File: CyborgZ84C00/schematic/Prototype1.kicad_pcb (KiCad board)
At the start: 2 copper layers, 4 parts, among them U1 Z84C00, U2 ATmega4809-P, U3 HM628128

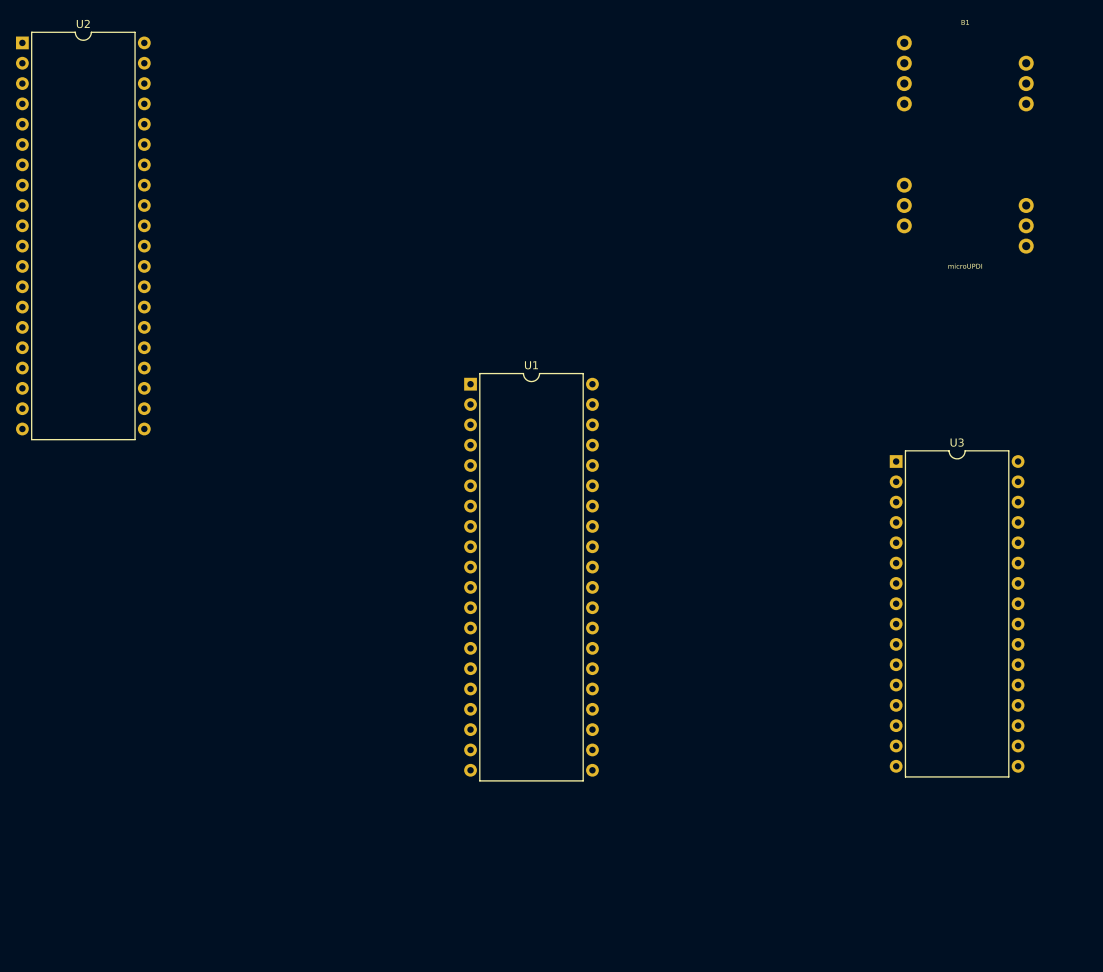
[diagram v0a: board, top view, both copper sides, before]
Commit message: [CyborgZ84C00] Update schematics symbols
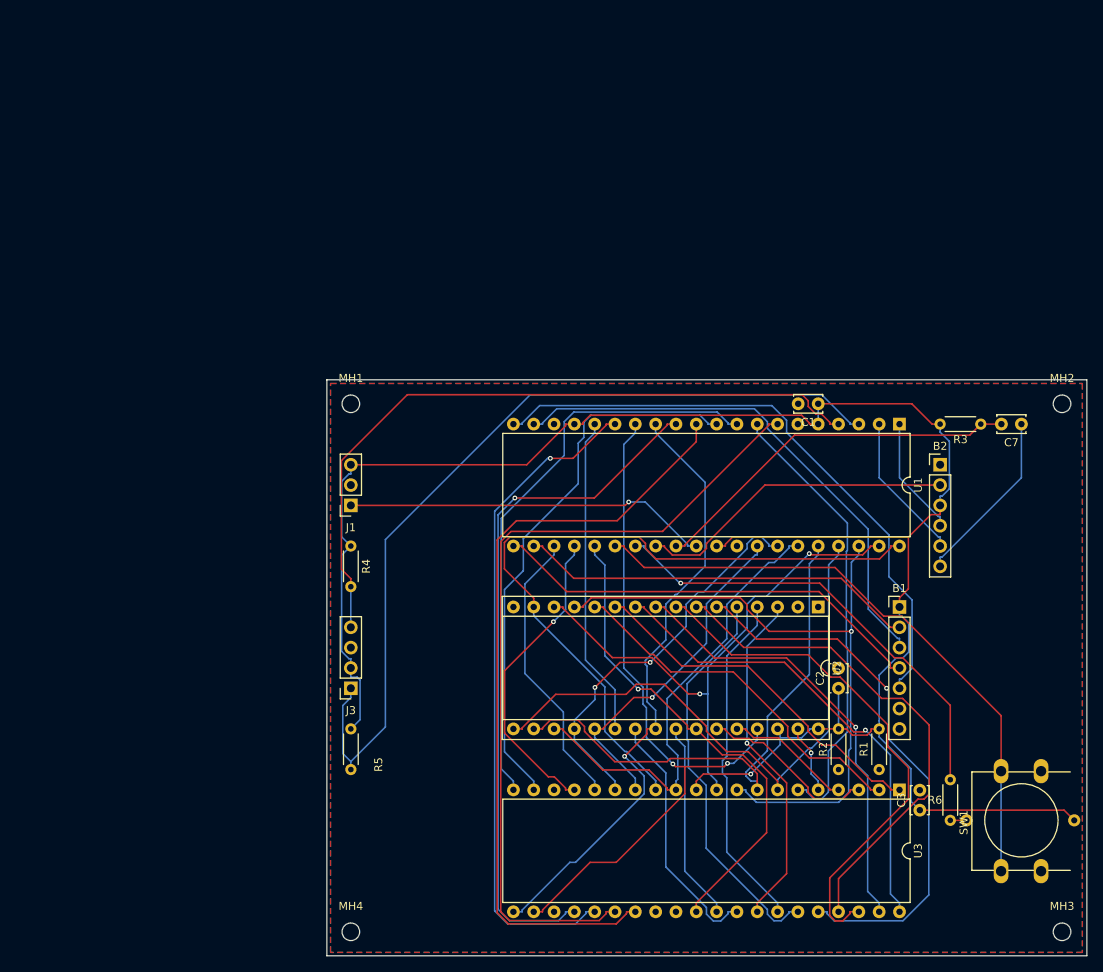
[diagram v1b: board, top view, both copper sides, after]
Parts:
- added B2: USB_Serial, 0-LocalLibrary:GY232V2, F.Cu at (174.7, 77.6)
- added C1: 0.1u, Capacitor_THT:C_Disc_D3.4mm_W2.1mm_P2.50mm, F.Cu at (159.4, 70.0)
- added C2: 0.1u, Capacitor_THT:C_Disc_D3.4mm_W2.1mm_P2.50mm, F.Cu at (162.0, 105.6)
- added C3: 0.1u, Capacitor_THT:C_Disc_D3.4mm_W2.1mm_P2.50mm, F.Cu at (172.1, 120.8)
- added C7: 0.1u, Capacitor_THT:C_Disc_D3.4mm_W2.1mm_P2.50mm, F.Cu at (184.8, 72.5)
- added J1: Conn_AVR_UPDI, Connector_PinSocket_2.54mm:PinSocket_1x03_P2.54mm_Vertical, F.Cu at (101.0, 82.7)
- added J3: Conn_I2C_Master, Connector_PinSocket_2.54mm:PinSocket_1x04_P2.54mm_Vertical, F.Cu at (101.0, 105.6)
- added MH1: MountingHole_2.2mm_M2, MountingHole:MountingHole_2.2mm_M2, F.Cu at (101.0, 70.0)
- added MH2: MountingHole_2.2mm_M2, MountingHole:MountingHole_2.2mm_M2, F.Cu at (189.9, 70.0)
- added MH3: MountingHole_2.2mm_M2, MountingHole:MountingHole_2.2mm_M2, F.Cu at (189.9, 136.0)
- added MH4: MountingHole_2.2mm_M2, MountingHole:MountingHole_2.2mm_M2, F.Cu at (101.0, 136.0)
- added R1: 10k, Resistor_THT:R_Axial_DIN0204_L3.6mm_D1.6mm_P5.08mm_Horizontal, F.Cu at (167.0, 115.7)
- added R2: 10k, Resistor_THT:R_Axial_DIN0204_L3.6mm_D1.6mm_P5.08mm_Horizontal, F.Cu at (162.0, 115.7)
- added R3: 10k, Resistor_THT:R_Axial_DIN0204_L3.6mm_D1.6mm_P5.08mm_Horizontal, F.Cu at (179.7, 72.5)
- added R4: 4k7, Resistor_THT:R_Axial_DIN0204_L3.6mm_D1.6mm_P5.08mm_Horizontal, F.Cu at (101.0, 87.8)
- added R5: 4k7, Resistor_THT:R_Axial_DIN0204_L3.6mm_D1.6mm_P5.08mm_Horizontal, F.Cu at (101.0, 110.6)
- added R6: 560, Resistor_THT:R_Axial_DIN0204_L3.6mm_D1.6mm_P5.08mm_Horizontal, F.Cu at (175.9, 122.1)
- added SW1: TSD1265, 0-LocalLibrary:SW_PUSH-LED-12mm, F.Cu at (182.3, 128.4)
- B1: value microUPDI -> Micro_SD; footprint 0-LocalLibrary:microUPDI -> 0-LocalLibrary:uSD_CARD
- U1: value Z84C00 -> ATmega4809-P
- U2: value ATmega4809-P -> HM628128DLP-5; footprint Package_DIP:DIP-40_W15.24mm -> Package_DIP:DIP-32_W15.24mm_Socket
- U3: value HM628128 -> Z84C00; footprint Package_DIP:DIP-32_W15.24mm -> Package_DIP:DIP-40_W15.24mm
- moved U2 121.9 mm to (159.4, 95.4), turned to 270 degrees
- moved B1 58.4 mm to (169.6, 95.4)
- moved U1 53.9 mm to (169.6, 72.5), turned to 270 degrees
- moved U3 41.0 mm to (169.6, 118.3), turned to 270 degrees
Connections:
- B1 pad 1: (no net) -> VCC
- B1 pad 2: (no net) -> /~SD_CS~
- B1 pad 3: (no net) -> /SD_DI
- B1 pad 4: (no net) -> /SD_SCK
- U1 pad 1: (no net) -> /DBG_RX
- U1 pad 10: (no net) -> /~MREQ~
- U1 pad 11: (no net) -> /~M1~
- U1 pad 12: (no net) -> /~WAIT~
- U1 pad 13: (no net) -> /~RD~
- U1 pad 14: (no net) -> /~WR~
- U1 pad 15: (no net) -> /~BUSREQ~
- U1 pad 16: (no net) -> /~RAM_E~
- U1 pad 17: (no net) -> VCC
- U1 pad 18: (no net) -> GND
- U1 pad 19: (no net) -> /SD_DI
- U1 pad 2: (no net) -> /DBG_TX
- U1 pad 20: (no net) -> /SD_DO
- U1 pad 21: (no net) -> /SD_SCK
- U1 pad 22: (no net) -> /~SD_CS~
- U1 pad 23: (no net) -> /~INT~
- U1 pad 24: (no net) -> /~NMI~
- U1 pad 25: (no net) -> /A0
- U1 pad 26: (no net) -> /~USR_SW~
- U1 pad 27: (no net) -> /~USR_LED~
- U1 pad 28: (no net) -> /~DBG_RTS~
- U1 pad 29: (no net) -> /~DBG_RESET~
- U1 pad 3: (no net) -> /SDA
- U1 pad 30: (no net) -> Net-(J1-Pad1)
- U1 pad 31: (no net) -> VCC
- U1 pad 32: (no net) -> GND
- U1 pad 33: (no net) -> /D0
- U1 pad 34: (no net) -> /D1
- U1 pad 35: (no net) -> /D2
- U1 pad 36: (no net) -> /D3
- U1 pad 37: (no net) -> /D4
- U1 pad 38: (no net) -> /D5
- U1 pad 39: (no net) -> /D6
- U1 pad 4: (no net) -> /SCL
- U1 pad 40: (no net) -> /D7
- U1 pad 5: (no net) -> VCC
- U1 pad 6: (no net) -> GND
- U1 pad 7: (no net) -> /~RESET~
- U1 pad 8: (no net) -> /CLK
- U1 pad 9: (no net) -> /~IORQ~
- U2 pad 10: (no net) -> /A10
- U2 pad 11: (no net) -> /A11
- U2 pad 12: (no net) -> /A12
- U2 pad 13: (no net) -> /D5
- U2 pad 14: (no net) -> /D6
- U2 pad 15: (no net) -> /D7
- U2 pad 16: (no net) -> GND
- U2 pad 17: (no net) -> /D4
- U2 pad 18: Net-(U2-Pad18) -> /D3
- U2 pad 19: (no net) -> /D2
- U2 pad 2: (no net) -> GND
- U2 pad 20: (no net) -> /D1
- U2 pad 21: (no net) -> /D0
- U2 pad 22: (no net) -> /~RAM_E~
- U2 pad 23: (no net) -> /A2
- U2 pad 24: (no net) -> /~RD~
- U2 pad 25: (no net) -> /A1
- U2 pad 26: (no net) -> /A0
- U2 pad 27: (no net) -> /A13
- U2 pad 28: (no net) -> /A14
- U2 pad 29: (no net) -> /~WR~
- U2 pad 3: (no net) -> /A3
- U2 pad 30: Net-(B1-Pad9) -> VCC
- U2 pad 31: Net-(U2-Pad31) -> /A15
- U2 pad 32: Net-(U2-Pad18) -> VCC
- U2 pad 4: (no net) -> /A4
- U2 pad 5: Net-(U2-Pad31) -> /A5
- U2 pad 6: Net-(U2-Pad18) -> /A6
- U2 pad 7: (no net) -> /A7
- U2 pad 8: (no net) -> /A8
- U2 pad 9: (no net) -> /A9
- U3 pad 1: (no net) -> /A11
- U3 pad 10: (no net) -> /D6
- U3 pad 11: (no net) -> VCC
- U3 pad 12: (no net) -> /D2
- U3 pad 13: (no net) -> /D7
- U3 pad 14: (no net) -> /D0
- U3 pad 15: (no net) -> /D1
- U3 pad 16: (no net) -> /~INT~
- U3 pad 17: (no net) -> /~NMI~
- U3 pad 18: (no net) -> Net-(U3-Pad18)
- U3 pad 19: (no net) -> /~MREQ~
- U3 pad 2: (no net) -> /A12
- U3 pad 20: (no net) -> /~IORQ~
- U3 pad 21: (no net) -> /~RD~
- U3 pad 22: (no net) -> /~WR~
- U3 pad 23: (no net) -> Net-(U3-Pad23)
- U3 pad 24: (no net) -> /~WAIT~
- U3 pad 25: (no net) -> /~BUSREQ~
- U3 pad 26: (no net) -> /~RESET~
- U3 pad 27: (no net) -> /~M1~
- U3 pad 28: (no net) -> Net-(U3-Pad28)
- U3 pad 29: (no net) -> GND
- U3 pad 3: (no net) -> /A13
- U3 pad 30: (no net) -> /A0
- U3 pad 31: (no net) -> /A1
- U3 pad 32: (no net) -> /A2
- U3 pad 4: (no net) -> /A14
- U3 pad 5: (no net) -> /A15
- U3 pad 6: (no net) -> /CLK
- U3 pad 7: (no net) -> /D4
- U3 pad 8: (no net) -> /D3
- U3 pad 9: (no net) -> /D5
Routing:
- net VCC: track 0.00 -> 253.1 mm, vias 0 -> 1
- net /SDA: track 0.00 -> 108.8 mm
- net /~RESET~: track 0.00 -> 102.4 mm
- net /~M1~: track 0.00 -> 97.4 mm
- net /D7: track 0.00 -> 90.8 mm
- net /SCL: track 0.00 -> 88.9 mm
- net /~WR~: track 0.00 -> 87.6 mm, vias 0 -> 2
- net /~WAIT~: track 0.00 -> 87.0 mm, vias 0 -> 1
- net /D5: track 0.00 -> 83.8 mm, vias 0 -> 1
- net /~BUSREQ~: track 0.00 -> 83.5 mm, vias 0 -> 1
- net /~RD~: track 0.00 -> 78.4 mm, vias 0 -> 1
- net /SD_DO: track 0.00 -> 76.7 mm
- net /~USR_SW~: track 0.00 -> 76.6 mm
- net /D4: track 0.00 -> 75.7 mm
- net /~IORQ~: track 0.00 -> 72.7 mm
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- added copper zone on B.Cu, net GND
- added copper zone on F.Cu, net GND
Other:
- board outline added: 95 x 72 mm
- net class Default: trace_width 0.25 -> 0.2; via_dia 0.8 -> 0.6; via_drill 0.4 -> 0.3
- rule trace_min: 0.2 -> 0.1524
- rule via_min_drill: 0.3 -> 0.2
- rule via_min_size: 0.4 -> 0.5

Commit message: [CyborgZ84C00] Update pin mapping
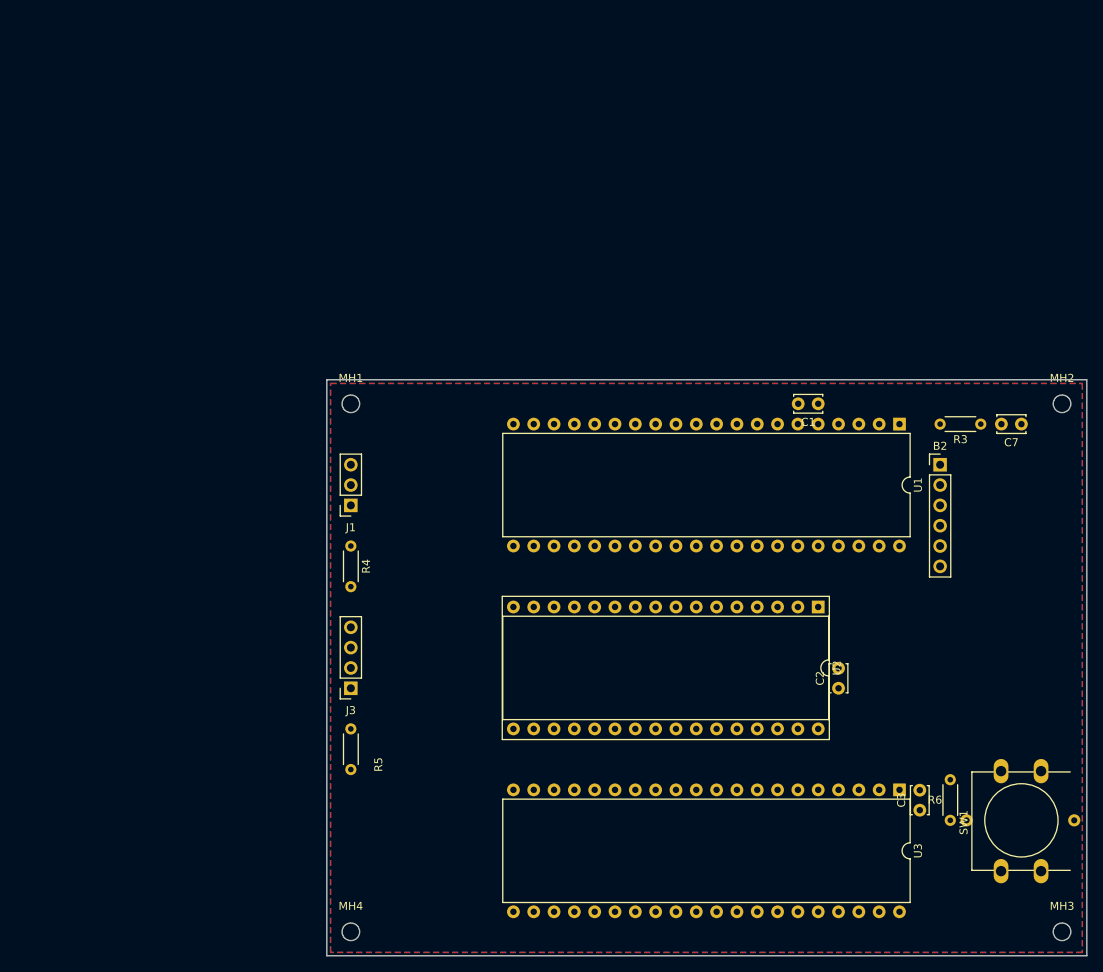
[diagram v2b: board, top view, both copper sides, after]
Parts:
- removed B1: Micro_SD, 0-LocalLibrary:uSD_CARD
- removed R1, R2: 10k, Resistor_THT:R_Axial_DIN0204_L3.6mm_D1.6mm_P5.08mm_Horizontal
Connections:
- U1 pad 10: /~MREQ~ -> /D1
- U1 pad 11: /~M1~ -> /D2
- U1 pad 12: /~WAIT~ -> /D3
- U1 pad 13: /~RD~ -> /D4
- U1 pad 14: /~WR~ -> /D5
- U1 pad 15: /~BUSREQ~ -> /D6
- U1 pad 16: /~RAM_E~ -> /D7
- U1 pad 19: /SD_DI -> (no net)
- U1 pad 20: /SD_DO -> (no net)
- U1 pad 21: /SD_SCK -> (no net)
- U1 pad 22: /~SD_CS~ -> (no net)
- U1 pad 26: /~USR_SW~ -> /A1
- U1 pad 27: /~USR_LED~ -> /~RESET~
- U1 pad 28: /~DBG_RTS~ -> /CLK
- U1 pad 3: /SDA -> /~RAM_E~
- U1 pad 33: /D0 -> /~IORQ~
- U1 pad 34: /D1 -> /~MREQ~
- U1 pad 35: /D2 -> /~M1~
- U1 pad 36: /D3 -> /~WAIT~
- U1 pad 37: /D4 -> /~RD~
- U1 pad 38: /D5 -> /~WR~
- U1 pad 39: /D6 -> /~BUSREQ~
- U1 pad 4: /SCL -> /~USR_SW~
- U1 pad 40: /D7 -> /~BUSACK~
- U1 pad 7: /~RESET~ -> /~USR_LED~
- U1 pad 8: /CLK -> /~DBG_RTS~
- U1 pad 9: /~IORQ~ -> /D0
- U3 pad 18: Net-(U3-Pad18) -> (no net)
- U3 pad 23: Net-(U3-Pad23) -> /~BUSACK~
- U3 pad 28: Net-(U3-Pad28) -> (no net)
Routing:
- net VCC: track 253.1 -> 0.00 mm, vias 1 -> 0
- net /SDA: track 108.8 -> 0.00 mm
- net /~RESET~: track 102.4 -> 0.00 mm
- net /~M1~: track 97.4 -> 0.00 mm
- net /D7: track 90.8 -> 0.00 mm
- net /SCL: track 88.9 -> 0.00 mm
- net /~WR~: track 87.6 -> 0.00 mm, vias 2 -> 0
- net /~WAIT~: track 87.0 -> 0.00 mm, vias 1 -> 0
- net /D5: track 83.8 -> 0.00 mm, vias 1 -> 0
- net /~BUSREQ~: track 83.5 -> 0.00 mm, vias 1 -> 0
- net /~RD~: track 78.4 -> 0.00 mm, vias 1 -> 0
- net /SD_DO: track 76.7 -> 0.00 mm
- net /~USR_SW~: track 76.6 -> 0.00 mm
- net /D4: track 75.7 -> 0.00 mm
- net /~IORQ~: track 72.7 -> 0.00 mm
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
